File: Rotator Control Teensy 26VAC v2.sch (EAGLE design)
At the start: 61 parts, among them K1 G5LE, K2 G5LE, K3 G5LE, Q1 BSS123, Q2 BSS123, Q3 BSS123, U2 MAX6959BAEE+, X1 Rotor, X2 26VAC

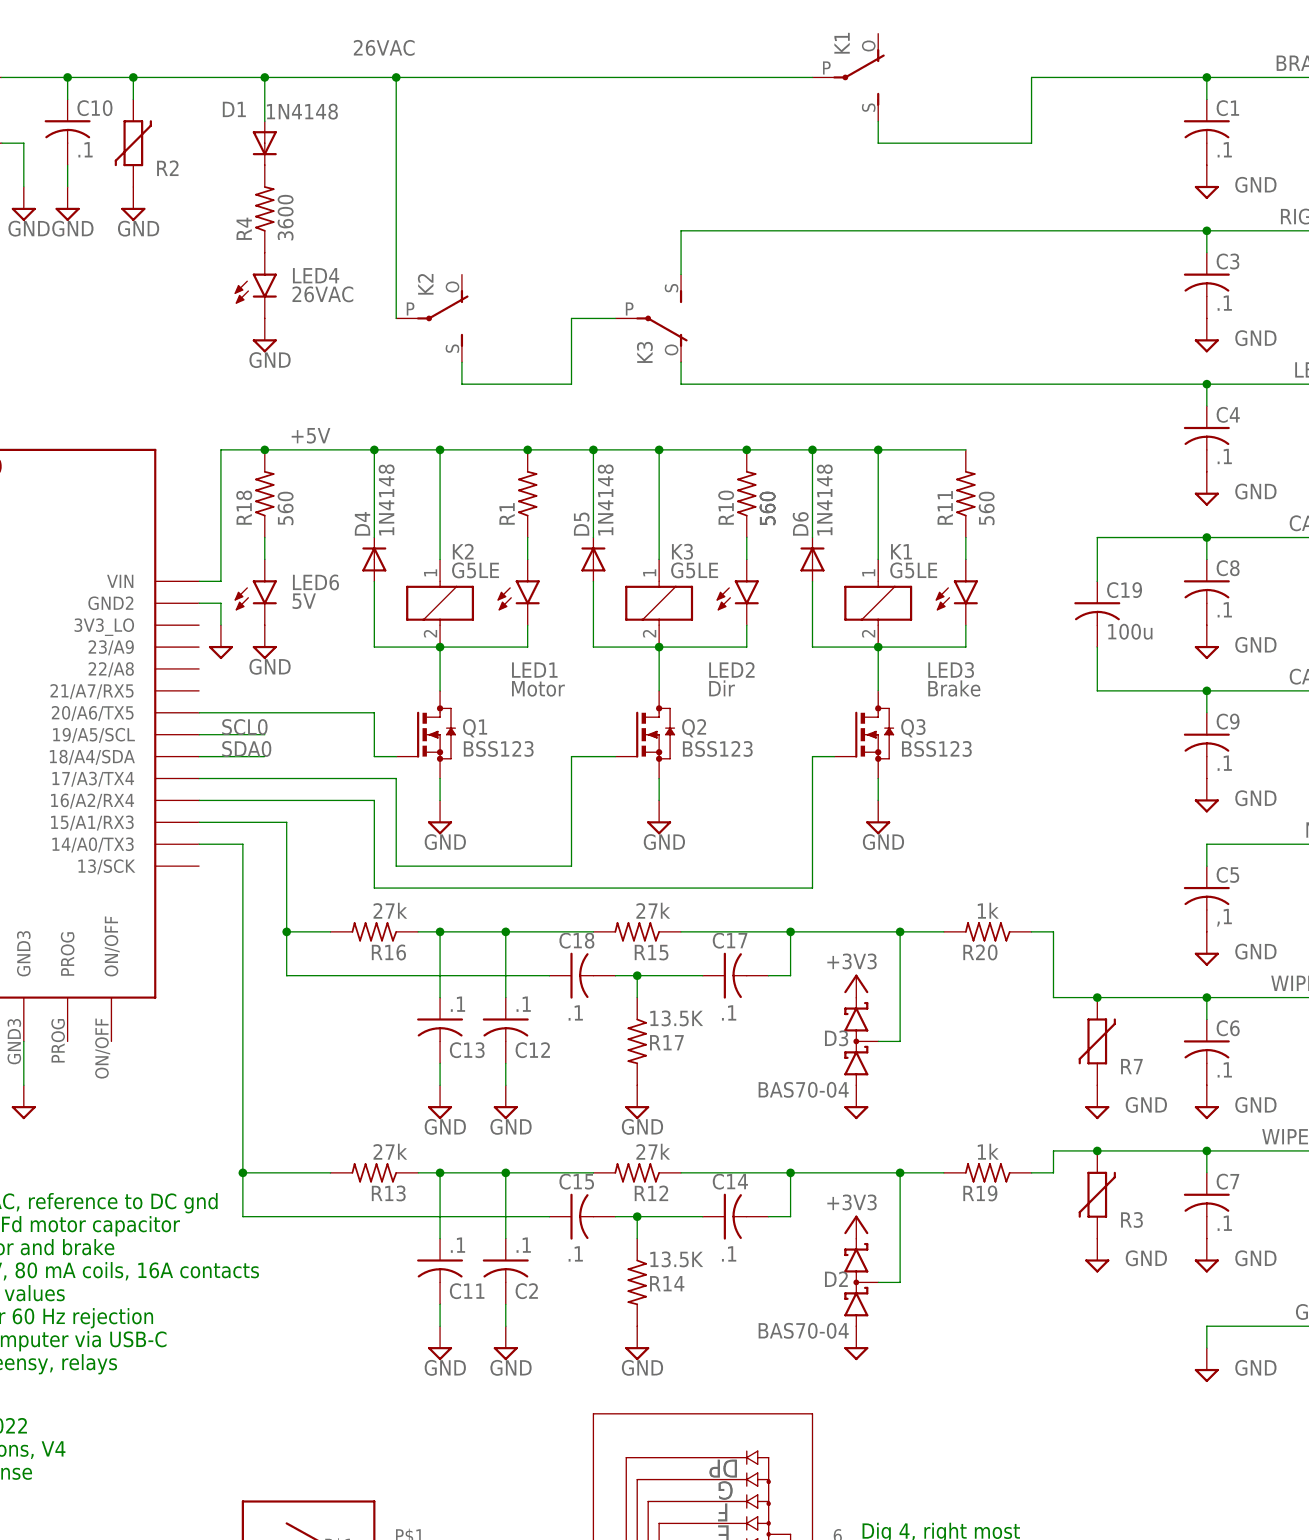
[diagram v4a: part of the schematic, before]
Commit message: Add 5V power supply resistors to the rotor pot leads
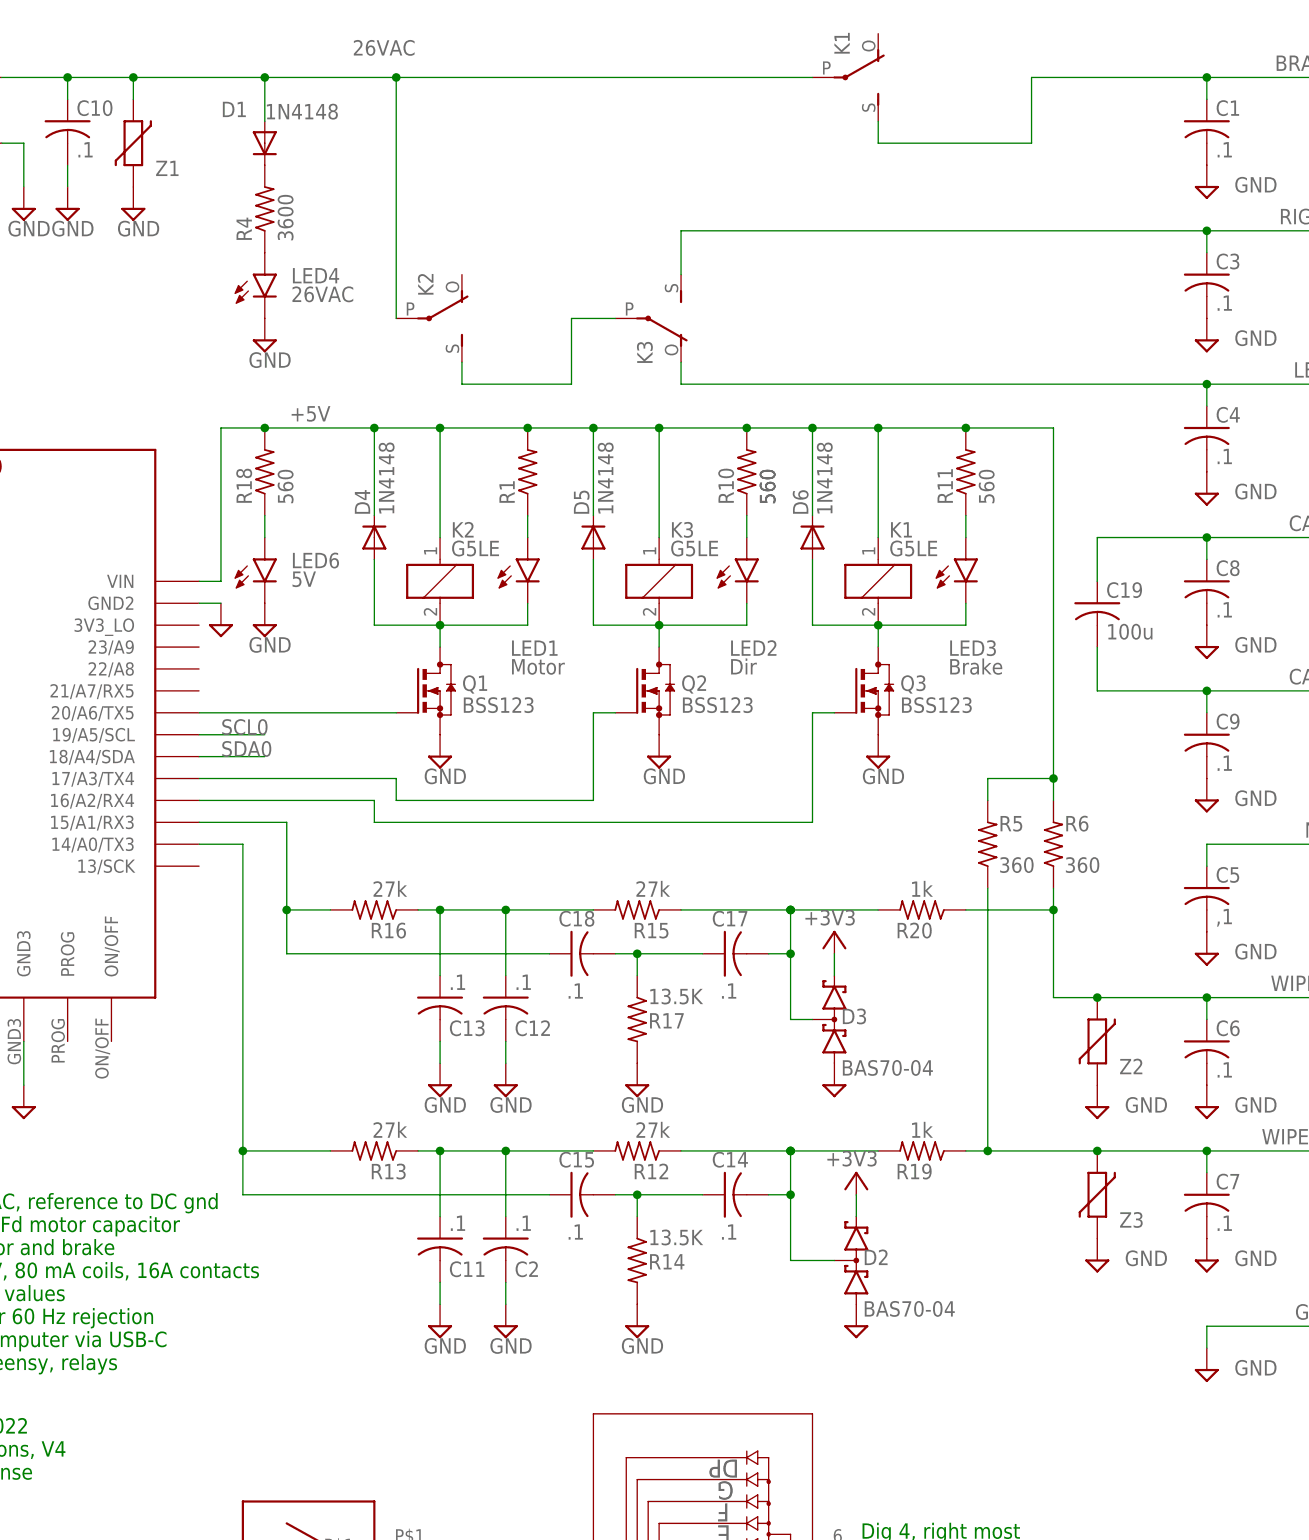
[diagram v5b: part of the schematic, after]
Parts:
- added R5, R6: 360, rcl:R-US_R0805
- renumbered R2 to Z1, R3 to Z3, R7 to Z2
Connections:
- net +5V: now also R5.2, R6.2
- net WIPER+: now also R5.1
- net WIPER-: now also R6.1
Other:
- moved on the sheet: C11, C12, C13, C14, C15, C17, C18, C2, D2, D3, D4, D5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

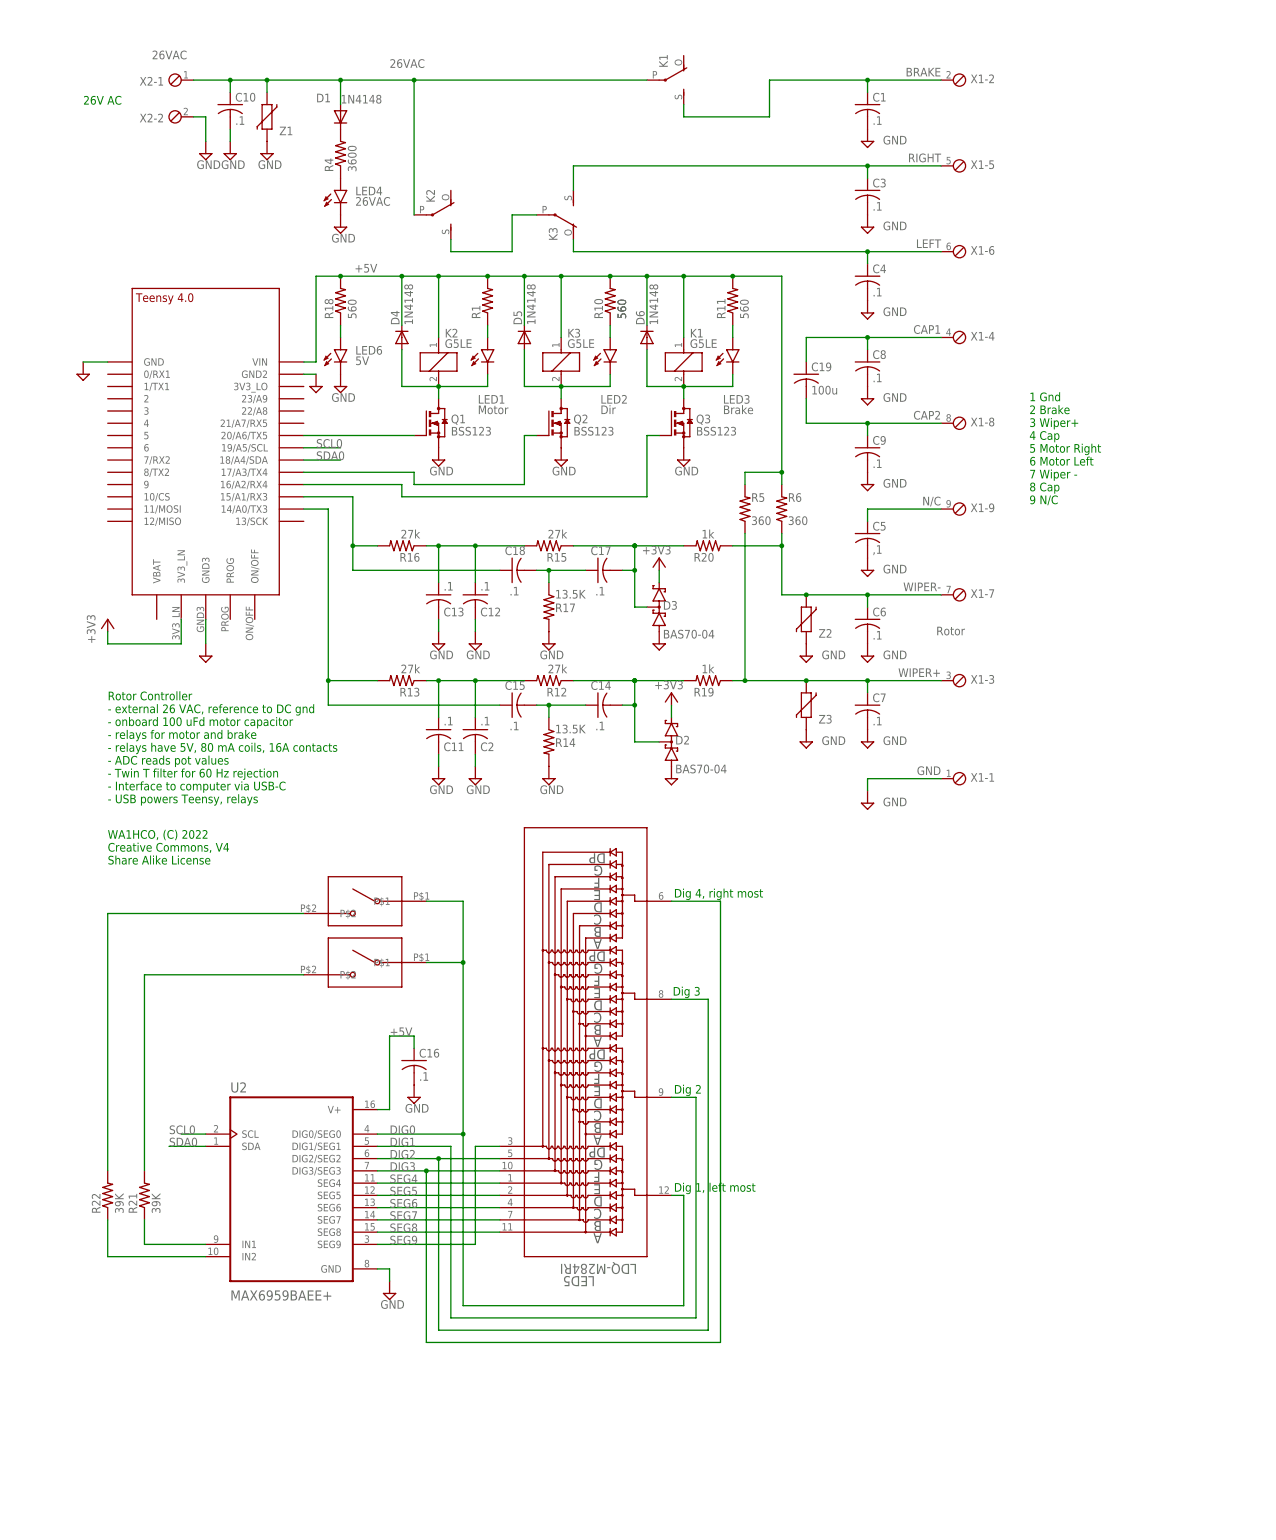
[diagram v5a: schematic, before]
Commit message: Add pullups on I2C lines Add holes for 7 segment LED with 0.4 in lead spacing
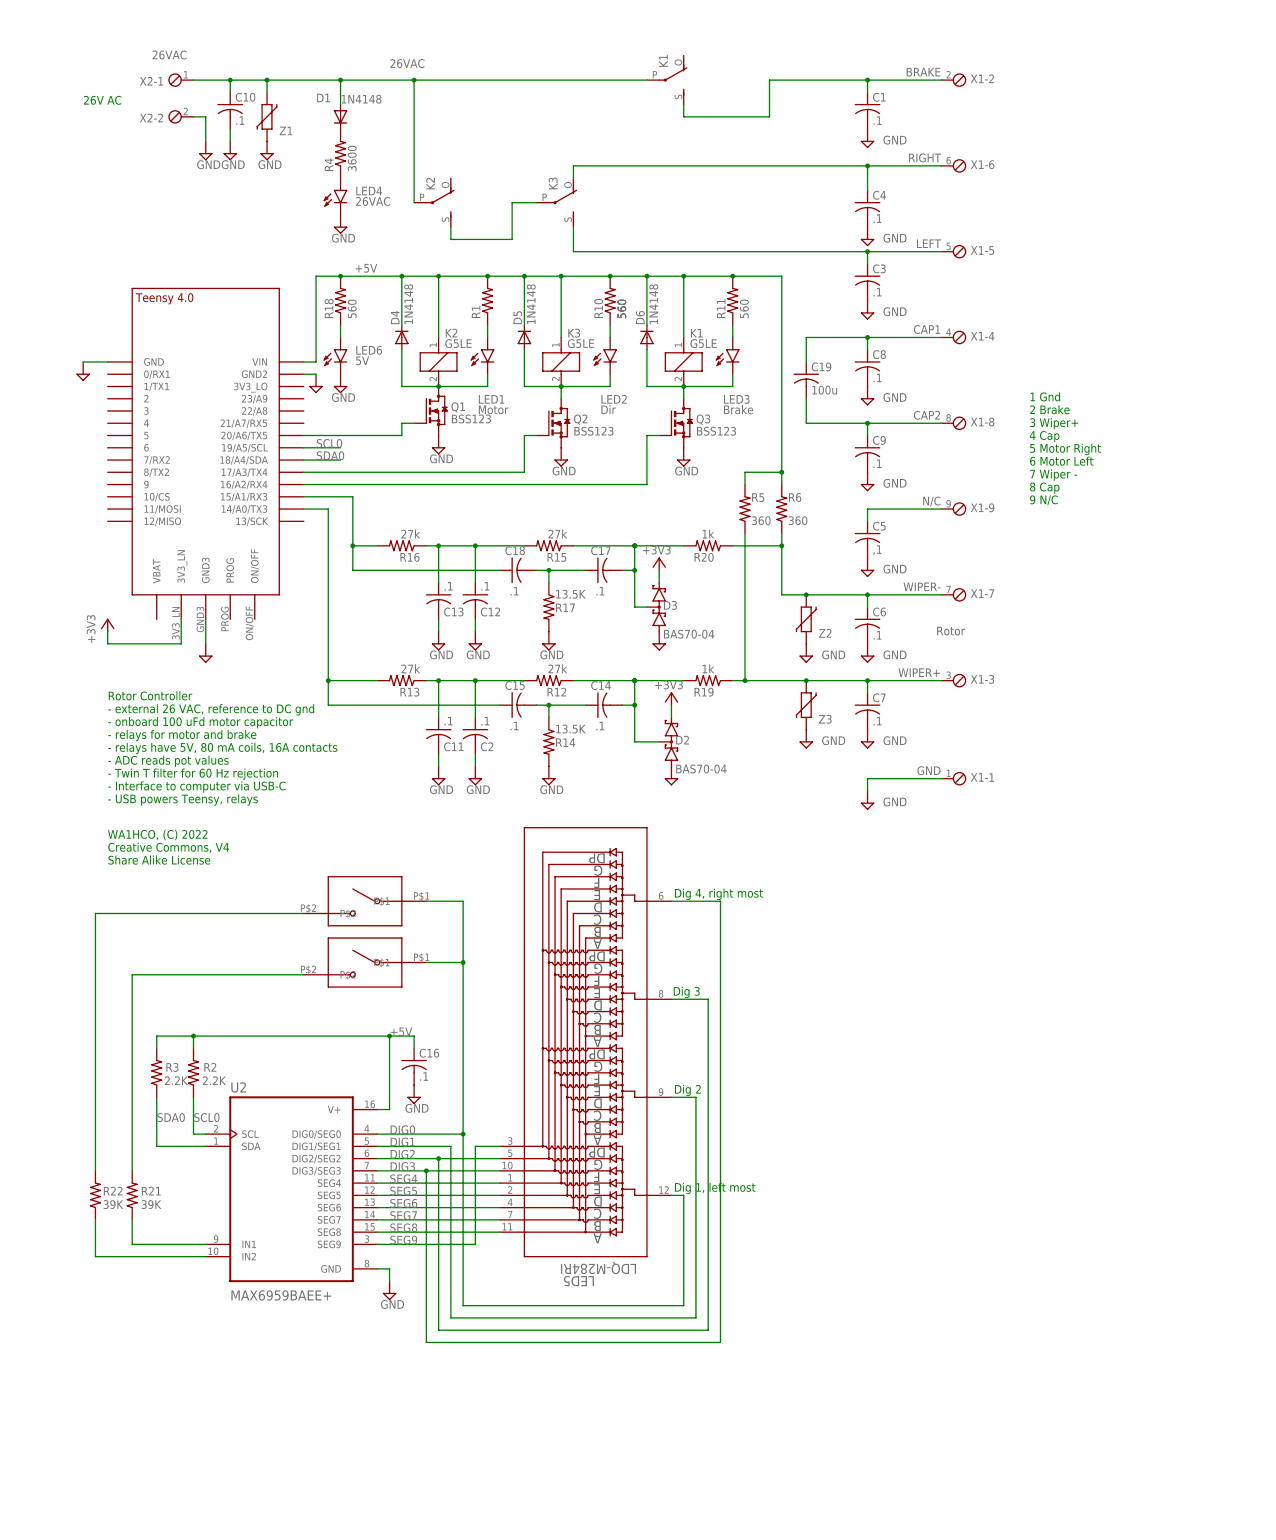
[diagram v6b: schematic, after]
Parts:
- added R2, R3: 2.2K, rcl:R-US_R0805
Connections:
- net +5V: now also R2.2, R3.2
- net SCL0: now also R2.1
- net SDA0: now also R3.1
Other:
- moved on the sheet: C3, C4, K2, K3, Q1, R21, R22, X1-5, X1-6

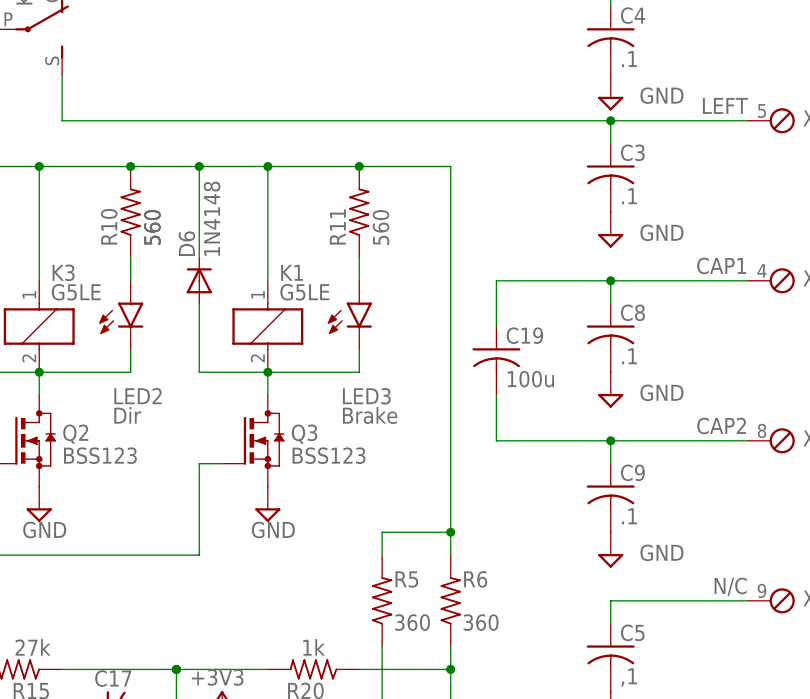
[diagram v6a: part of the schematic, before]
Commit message: move rotator pot pullups from 5V to regulated 3.3V.  5V varied from USB to USB and changed when relays activated...which changed the azimuth calibration
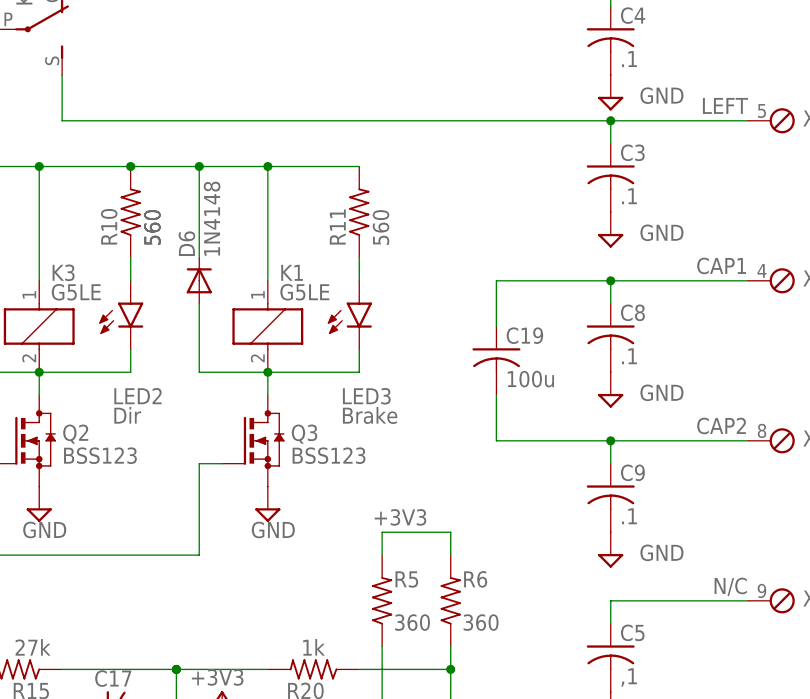
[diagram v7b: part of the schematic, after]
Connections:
- net +3V3: now also R5.2, R6.2
- net +5V: no longer R5.2, R6.2
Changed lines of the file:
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@@
 <wire x1="152.4" y1="17.78" x2="152.4" y2="20.32" width="0.1524" layer="91"/>
+</segment>
+<segment>
+<pinref part="R6" gate="G$1" pin="2"/>
+<wire x1="177.8" y1="40.64" x2="177.8" y2="38.1" width="0.1524" layer="91"/>
+<pinref part="R5" gate="G$1" pin="2"/>
+<wire x1="170.18" y1="38.1" x2="170.18" y2="40.64" width="0.1524" layer="91"/>
+<wire x1="170.18" y1="40.64" x2="177.8" y2="40.64" width="0.1524" layer="91"/>
+<label x="175.26" y="43.18" size="1.778" layer="95" rot="R180"/>
 </segment>
 </net>
@@
 <junction x="142.24" y="81.28"/>
 <junction x="149.86" y="81.28"/>
-<wire x1="167.64" y1="81.28" x2="177.8" y2="81.28" width="0.1524" layer="91"/>
-<junction x="167.64" y="81.28"/>
-<pinref part="R6" gate="G$1" pin="2"/>
-<wire x1="177.8" y1="81.28" x2="177.8" y2="40.64" width="0.1524" layer="91"/>
-<pinref part="R5" gate="G$1" pin="2"/>
-<wire x1="177.8" y1="40.64" x2="177.8" y2="38.1" width="0.1524" layer="91"/>
-<wire x1="170.18" y1="38.1" x2="170.18" y2="40.64" width="0.1524" layer="91"/>
-<wire x1="170.18" y1="40.64" x2="177.8" y2="40.64" width="0.1524" layer="91"/>
-<junction x="177.8" y="40.64"/>
 </segment>
 <segment>
